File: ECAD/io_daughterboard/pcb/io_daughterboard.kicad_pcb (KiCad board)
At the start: 2 copper layers, 120 x 66 mm, 90 parts, among them CON1 BARREL_JACK, J1 XF2L-0625-1A, J2 4-1734839-0, P1 CONN_02X32, P10 Slave 5B, P11 Slave 1C, P12 Slave 3C, P13 Slave 4C, P14 Slave 5C, P15 Slave 1D, P16 Slave 3D, P17 Slave 4D, P18 Slave 5D, P2 CONN_02X32, P3 Slave 1A, P4 Slave 3A, P5 Slave 4A, P6 Slave 5A, P7 Slave 1B, P8 Slave 3B, P9 Slave 4B, U1 FAN5333BSX, U10 SN74LV1T34DCKR, U11 SN74LV1T34DCKR, U2 SPX3819M5-L-3-3, U3 74HC244, U4 74HC244, U5 74HC244, U6 STMPE811QTR, U7 74HC244, U8 74HC244, U9 74HC244

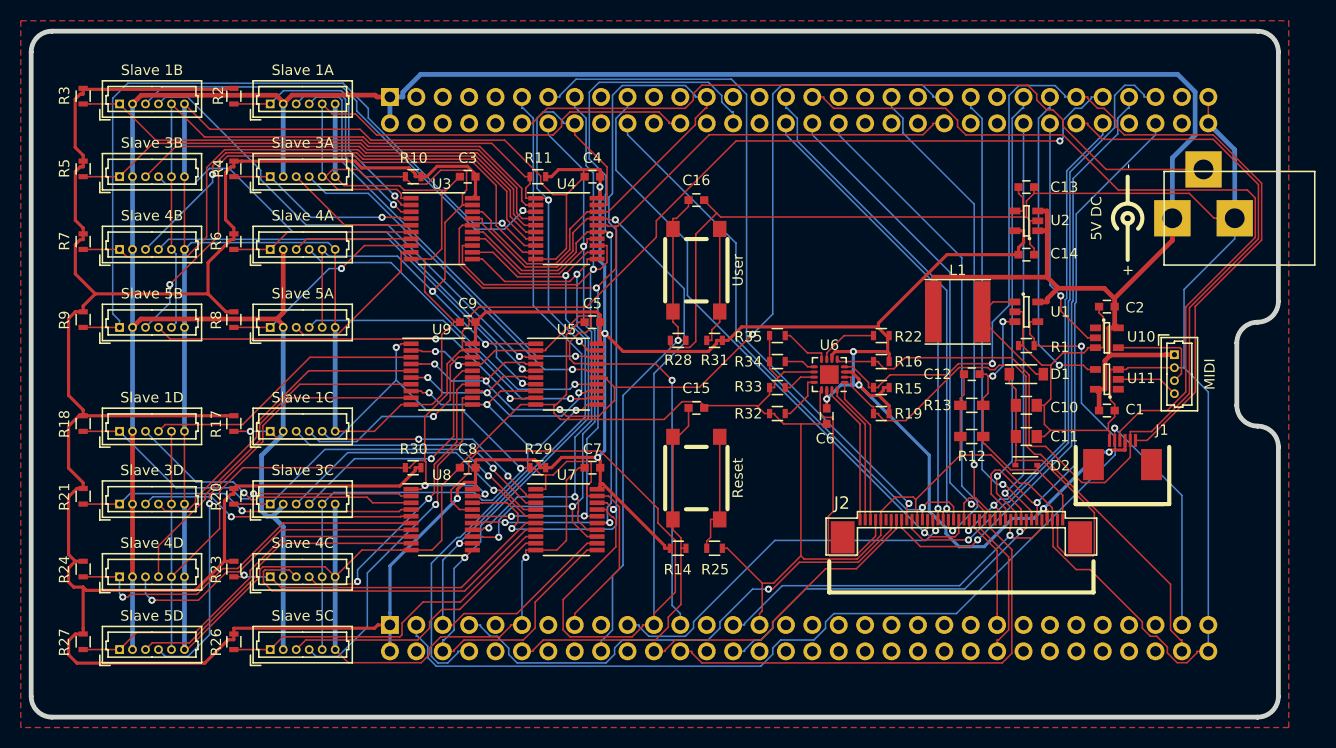
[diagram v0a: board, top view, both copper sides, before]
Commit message: Removed all traces and vias (again).
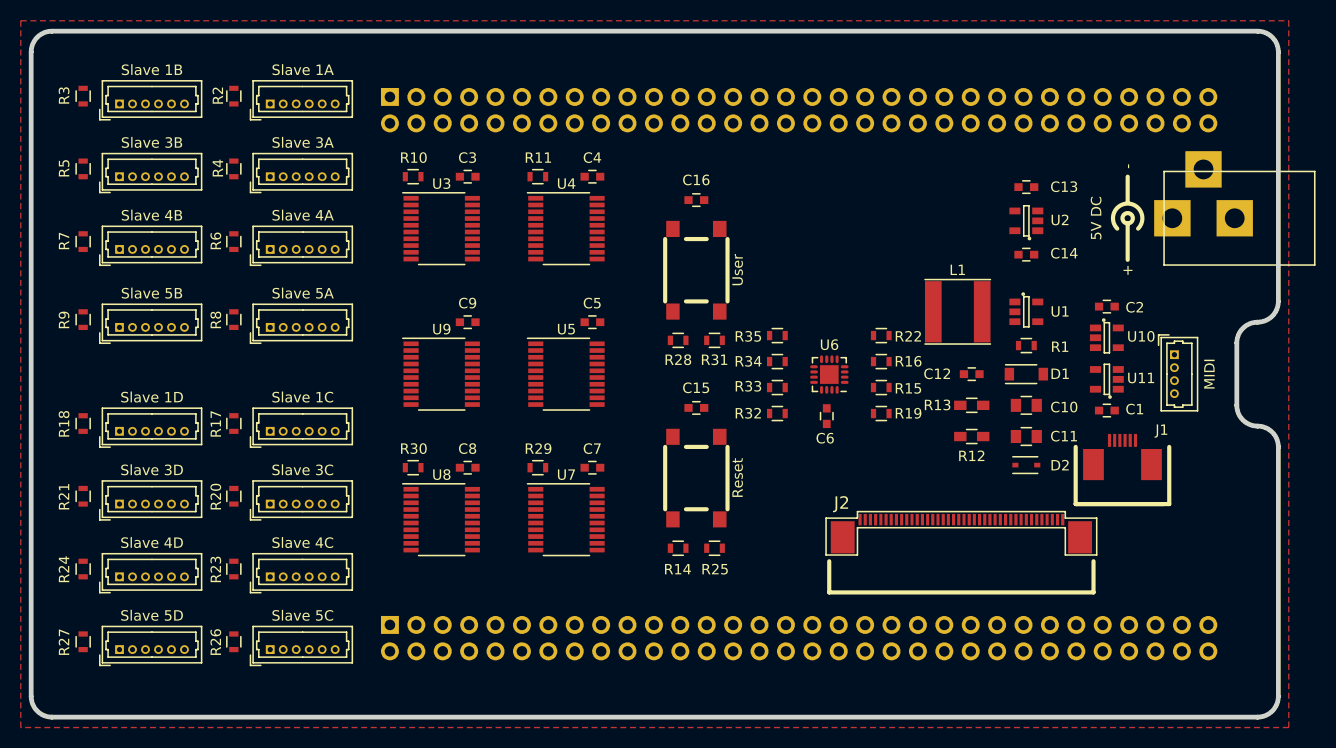
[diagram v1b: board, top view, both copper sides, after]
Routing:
- net GND: track 622.0 -> 0.00 mm, vias 1 -> 0
- net +3V3: track 444.0 -> 0.00 mm, vias 9 -> 0
- net +5V: track 299.1 -> 0.00 mm
- net /PC8: track 152.0 -> 0.00 mm, vias 3 -> 0
- net /PA5: track 127.1 -> 0.00 mm, vias 1 -> 0
- net /PB7: track 115.1 -> 0.00 mm, vias 2 -> 0
- net /PB4: track 104.5 -> 0.00 mm, vias 2 -> 0
- net /PE3: track 103.6 -> 0.00 mm, vias 2 -> 0
- net /I²C3_SCL: track 102.4 -> 0.00 mm, vias 1 -> 0
- net /LCD_PWM: track 98.9 -> 0.00 mm, vias 1 -> 0
- net /PC11: track 97.9 -> 0.00 mm, vias 3 -> 0
- net /PC3: track 95.4 -> 0.00 mm, vias 2 -> 0
- net /I²C3_SDA: track 91.6 -> 0.00 mm
- net /PB3: track 90.8 -> 0.00 mm, vias 3 -> 0
- net /PC12: track 89.6 -> 0.00 mm, vias 4 -> 0
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
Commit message: Delete ground zone.  Added traces for filter capacitors.
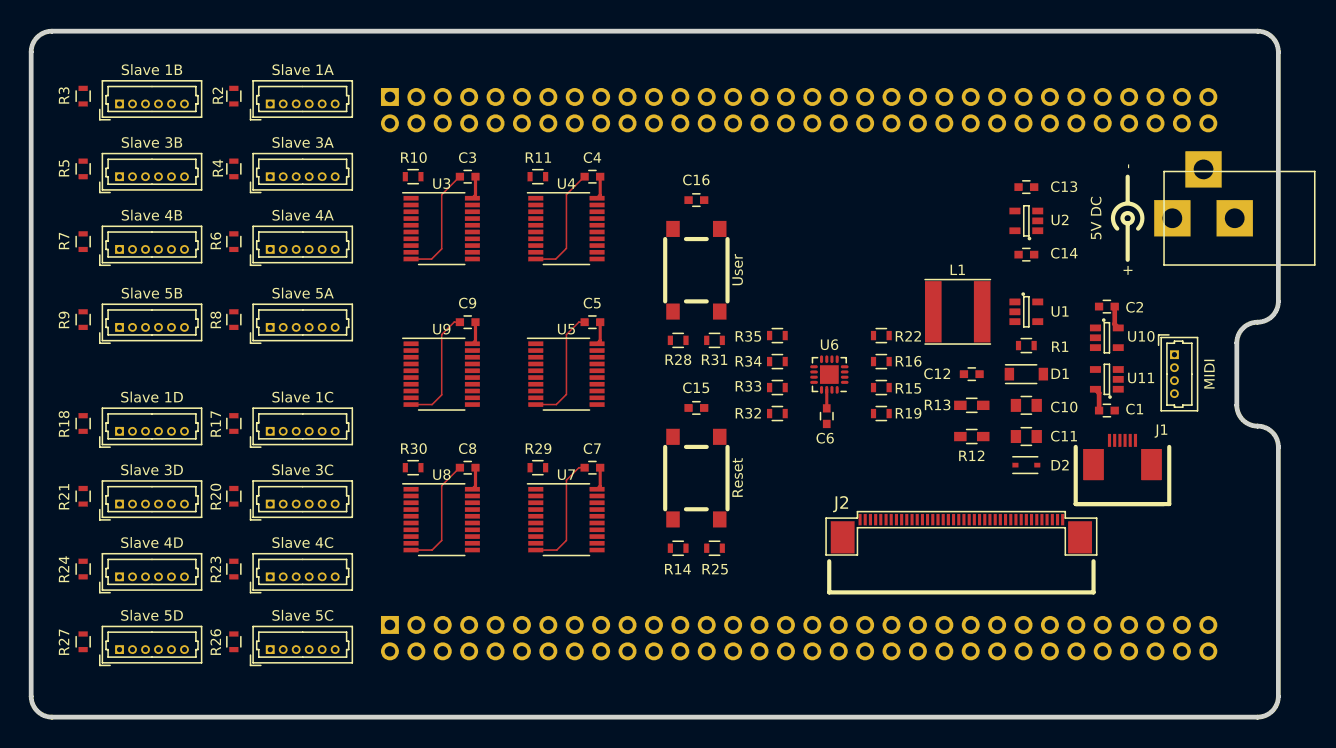
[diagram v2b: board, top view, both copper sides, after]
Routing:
- net GND: track 0.00 -> 67.2 mm
- net +3V3: track 0.00 -> 15.0 mm
- net +5V: track 0.00 -> 4.39 mm
- removed copper zone on F.Cu, net GND
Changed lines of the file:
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@@
   (general
     (links 360)
-    (no_connects 0)
+    (no_connects 345)
     (area 84.650001 26.3 231.421429 122.700001)
     (thickness 1.6)
     (drawings 24)
-    (tracks 2126)
+    (tracks 47)
     (zones 0)
     (modules 90)
@@
   )
   (layers
-    (0 F.Cu signal hide)
+    (0 F.Cu signal)
     (31 B.Cu signal)
     (34 B.Paste user)
-    (35 F.Paste user hide)
+    (35 F.Paste user)
     (36 B.SilkS user)
     (37 F.SilkS user)
-    (38 B.Mask user hide)
-    (39 F.Mask user hide)
+    (38 B.Mask user)
+    (39 F.Mask user)
     (40 Dwgs.User user)
     (44 Edge.Cuts user)
@@
   (gr_line (start 102 34) (end 218 34) (angle -90) (layer Edge.Cuts) (width 0.4572))
   (gr_line (start 218 100) (end 102 100) (angle -90) (layer Edge.Cuts) (width 0.4572))
-  (zone (net 2) (net_name GND) (layer F.Cu) (hatch edge 0.508)
-    (connect_pads (clearance 0.1524))
-    (min_thickness 0.1524)
-    (fill yes (arc_segments 16) (thermal_gap 0.1524) (thermal_bridge_width 0.508))
-    (polygon
-      (pts
-        (xy 99 33) (xy 221 33) (xy 221 101) (xy 99 101)
-      )
-    )
-  )
+  (segment (start 202.75 70.5) (end 202.75 68.8) (width 0.4572) (layer F.Cu) (net 1))
+  (segment (start 202.75 68.8) (end 202.4 68.45) (width 0.4572) (layer F.Cu) (net 1))
+  (segment (start 204.25 60.5) (end 204.25 62.2) (width 0.4572) (layer F.Cu) (net 1))
+  (segment (start 204.25 62.2) (end 204.6 62.55) (width 0.4572) (layer F.Cu) (net 1))
+  (segment (start 139.5 83) (end 138.575 83.925) (width 0.1524) (layer F.Cu) (net 2))
+  (segment (start 138.575 83.925) (end 136.55 83.925) (width 0.1524) (layer F.Cu) (net 2))
+  (segment (start 139.5 77.725) (end 139.5 83) (width 0.1524) (layer F.Cu) (net 2))
+  (segment (start 141.25 76) (end 141.225 76) (width 0.1524) (layer F.Cu) (net 2))
+  (segment (start 141.225 76) (end 139.5 77.725) (width 0.1524) (layer F.Cu) (net 2))
+  (segment (start 151.5 83) (end 150.575 83.925) (width 0.1524) (layer F.Cu) (net 2))
+  (segment (start 150.575 83.925) (end 148.55 83.925) (width 0.1524) (layer F.Cu) (net 2))
+  (segment (start 151.5 77.1976) (end 151.5 83) (width 0.1524) (layer F.Cu) (net 2))
+  (segment (start 153.25 76) (end 152.6976 76) (width 0.1524) (layer F.Cu) (net 2))
+  (segment (start 152.6976 76) (end 151.5 77.1976) (width 0.1524) (layer F.Cu) (net 2))
+  (segment (start 139.5 69) (end 138.575 69.925) (width 0.1524) (layer F.Cu) (net 2))
+  (segment (start 138.575 69.925) (end 136.55 69.925) (width 0.1524) (layer F.Cu) (net 2))
+  (segment (start 139.5 63.1976) (end 139.5 69) (width 0.1524) (layer F.Cu) (net 2))
+  (segment (start 141.25 62) (end 140.6976 62) (width 0.1524) (layer F.Cu) (net 2))
+  (segment (start 140.6976 62) (end 139.5 63.1976) (width 0.1524) (layer F.Cu) (net 2))
+  (segment (start 151.5 68.95) (end 150.525 69.925) (width 0.1524) (layer F.Cu) (net 2))
+  (segment (start 150.525 69.925) (end 148.55 69.925) (width 0.1524) (layer F.Cu) (net 2))
+  (segment (start 151.5 63.1976) (end 151.5 68.95) (width 0.1524) (layer F.Cu) (net 2))
+  (segment (start 153.25 62) (end 152.6976 62) (width 0.1524) (layer F.Cu) (net 2))
+  (segment (start 152.6976 62) (end 151.5 63.1976) (width 0.1524) (layer F.Cu) (net 2))
+  (segment (start 151.5 54.9) (end 150.475 55.925) (width 0.1524) (layer F.Cu) (net 2))
+  (segment (start 150.475 55.925) (end 148.55 55.925) (width 0.1524) (layer F.Cu) (net 2))
+  (segment (start 151.5 49.725) (end 151.5 54.9) (width 0.1524) (layer F.Cu) (net 2))
+  (segment (start 153.25 48) (end 153.225 48) (width 0.1524) (layer F.Cu) (net 2))
+  (segment (start 153.225 48) (end 151.5 49.725) (width 0.1524) (layer F.Cu) (net 2))
+  (segment (start 141.25 48) (end 141.225 48) (width 0.1524) (layer F.Cu) (net 2))
+  (segment (start 141.225 48) (end 139.5 49.725) (width 0.1524) (layer F.Cu) (net 2))
+  (segment (start 139.5 49.725) (end 139.5 54.95) (width 0.1524) (layer F.Cu) (net 2))
+  (segment (start 139.5 54.95) (end 138.525 55.925) (width 0.1524) (layer F.Cu) (net 2))
+  (segment (start 138.525 55.925) (end 136.55 55.925) (width 0.1524) (layer F.Cu) (net 2))
+  (segment (start 176.547 70.2892) (end 176.547 68.5142) (width 0.3048) (layer F.Cu) (net 3))
+  (segment (start 142.75 76) (end 142.75 77.775) (width 0.3048) (layer F.Cu) (net 3))
+  (segment (start 142.75 77.775) (end 142.45 78.075) (width 0.3048) (layer F.Cu) (net 3))
+  (segment (start 154.75 76) (end 154.75 77.775) (width 0.3048) (layer F.Cu) (net 3))
+  (segment (start 154.75 77.775) (end 154.45 78.075) (width 0.3048) (layer F.Cu) (net 3))
+  (segment (start 142.75 62) (end 142.75 63.775) (width 0.3048) (layer F.Cu) (net 3))
+  (segment (start 142.75 63.775) (end 142.45 64.075) (width 0.3048) (layer F.Cu) (net 3))
+  (segment (start 154.75 62) (end 154.75 63.775) (width 0.3048) (layer F.Cu) (net 3))
+  (segment (start 154.75 63.775) (end 154.45 64.075) (width 0.3048) (layer F.Cu) (net 3))
+  (segment (start 154.75 48) (end 154.75 49.775) (width 0.3048) (layer F.Cu) (net 3))
+  (segment (start 154.75 49.775) (end 154.45 50.075) (width 0.3048) (layer F.Cu) (net 3))
+  (segment (start 142.75 48) (end 142.75 49.775) (width 0.3048) (layer F.Cu) (net 3))
+  (segment (start 142.75 49.775) (end 142.45 50.075) (width 0.3048) (layer F.Cu) (net 3))
 )

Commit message: Changed solder mask clearance to 0.05 mm.  (Grrr!)
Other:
- rule pad_to_mask_clearance: 0.2 -> 0.05
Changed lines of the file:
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@@
     (pad_size 1.524 1.524)
     (pad_drill 0.762)
-    (pad_to_mask_clearance 0.2)
+    (pad_to_mask_clearance 0.05)
     (aux_axis_origin 0 0)
     (grid_origin 100 100)

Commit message: Moved J1 and J2 side by side.
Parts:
- moved J1 8.32 mm to (201.6, 81.6)
- moved J2 5.72 mm to (183.8, 81.0)
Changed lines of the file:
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@@
     (aux_axis_origin 0 0)
     (grid_origin 100 100)
-    (visible_elements FFFFEF7F)
+    (visible_elements FFFFFF7F)
     (pcbplotparams
       (layerselection 0x00030_80000001)
@@
   )
   (module daughterfeet:FPC_40 locked (layer F.Cu)
-    (at 189.5 81)
+    (at 183.78 81)
     (fp_text reference J2 (at -11.5 -1.6) (layer F.SilkS)
       (effects (font (size 1.2 1.2) (thickness 0.15)))
@@
   )
   (module daughterfeet:XF2L-0625 locked (layer F.Cu)
-    (at 205 74)
+    (at 201.61 81.6)
     (fp_text reference J1 (at 3.8 -1.625) (layer F.SilkS)
       (effects (font (size 1 1) (thickness 0.15)))
@@
   (gr_line (start 173.89 32) (end 173.89 102) (layer Dwgs.User) (width 0.03))
   (gr_line (start 220 67) (end 96 67) (angle 90) (layer Dwgs.User) (width 0.03))
-  (dimension 13.5 (width 0.03) (layer Dwgs.User)
-    (gr_text "13.5 mm" (at 213.25 111.35) (layer Dwgs.User)
+  (dimension 16.9 (width 0.03) (layer Dwgs.User)
+    (gr_text "16.8 mm" (at 213.25 111.35) (layer Dwgs.User)
       (effects (font (size 1.5 1.5) (thickness 0.3)))
     )
-    (feature1 (pts (xy 206.5 88) (xy 206.5 112.7)))
-    (feature2 (pts (xy 220 88) (xy 220 112.7)))
-    (crossbar (pts (xy 220 110) (xy 206.5 110)))
-    (arrow1a (pts (xy 206.5 110) (xy 207.627 110.586421)))
-    (arrow1b (pts (xy 206.5 110) (xy 207.627 109.413579)))
+    (feature1 (pts (xy 203.1 85) (xy 203.1 112.7)))
+    (feature2 (pts (xy 220 85) (xy 220 112.7)))
+    (crossbar (pts (xy 220 110) (xy 203.1 110)))
+    (arrow1a (pts (xy 203.1 110) (xy 204.227 110.586421)))
+    (arrow1b (pts (xy 203.1 110) (xy 24.227 109.413579)))
     (arrow2a (pts (xy 220 110) (xy 218.873 110.586421)))
     (arrow2b (pts (xy 220 110) (xy 218.873 109.413579)))
   )
-  (dimension 20.6 (width 0.03) (layer Dwgs.User)
-    (gr_text "20.6 mm" (at 209.75 116.35) (layer Dwgs.User)
+  (dimension 26 (width 0.03) (layer Dwgs.User)
+    (gr_text "26.0 mm" (at 209.75 116.35) (layer Dwgs.User)
       (effects (font (size 1.5 1.5) (thickness 0.3)))
     )
-    (feature1 (pts (xy 199.4 88) (xy 199.4 117.7)))
-    (feature2 (pts (xy 220 88) (xy 220 117.7)))
-    (crossbar (pts (xy 220 115) (xy 199.4 115)))
-    (arrow1a (pts (xy 199.4 115) (xy 200.627 115.586421)))
-    (arrow1b (pts (xy 199.4 115) (xy 200.627 114.413579)))
+    (feature1 (pts (xy 194 85) (xy 194 117.7)))
+    (feature2 (pts (xy 220 85) (xy 220 117.7)))
+    (crossbar (pts (xy 220 115) (xy 194 115)))
+    (arrow1a (pts (xy 194 115) (xy 195.227 115.586421)))
+    (arrow1b (pts (xy 194 115) (xy 195.227 114.413579)))
     (arrow2a (pts (xy 220 115) (xy 218.873 115.586421)))
     (arrow2b (pts (xy 220 115) (xy 218.873 114.413579)))

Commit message: Changed LCD connector to Hirose FH12A.
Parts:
- LCD: renamed from J2; value 4-1734839-0 -> FH12A-40S-0.5SH; footprint daughterfeet:FPC_40 -> daughterfeet:FH12A-40S
- renumbered J1 to CTouch
